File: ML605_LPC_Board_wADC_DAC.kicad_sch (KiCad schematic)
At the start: 19 parts, among them J1 ASP-134604-01, J10 Conn_02x06_Odd_Even, J11 Conn_02x06_Odd_Even, J12 Conn_02x06_Odd_Even, J2 Conn_01x03_Pin, J3 Conn_01x03_Pin, U1 LMV7219M7, U2 LMV7219M7, U3 NCV317

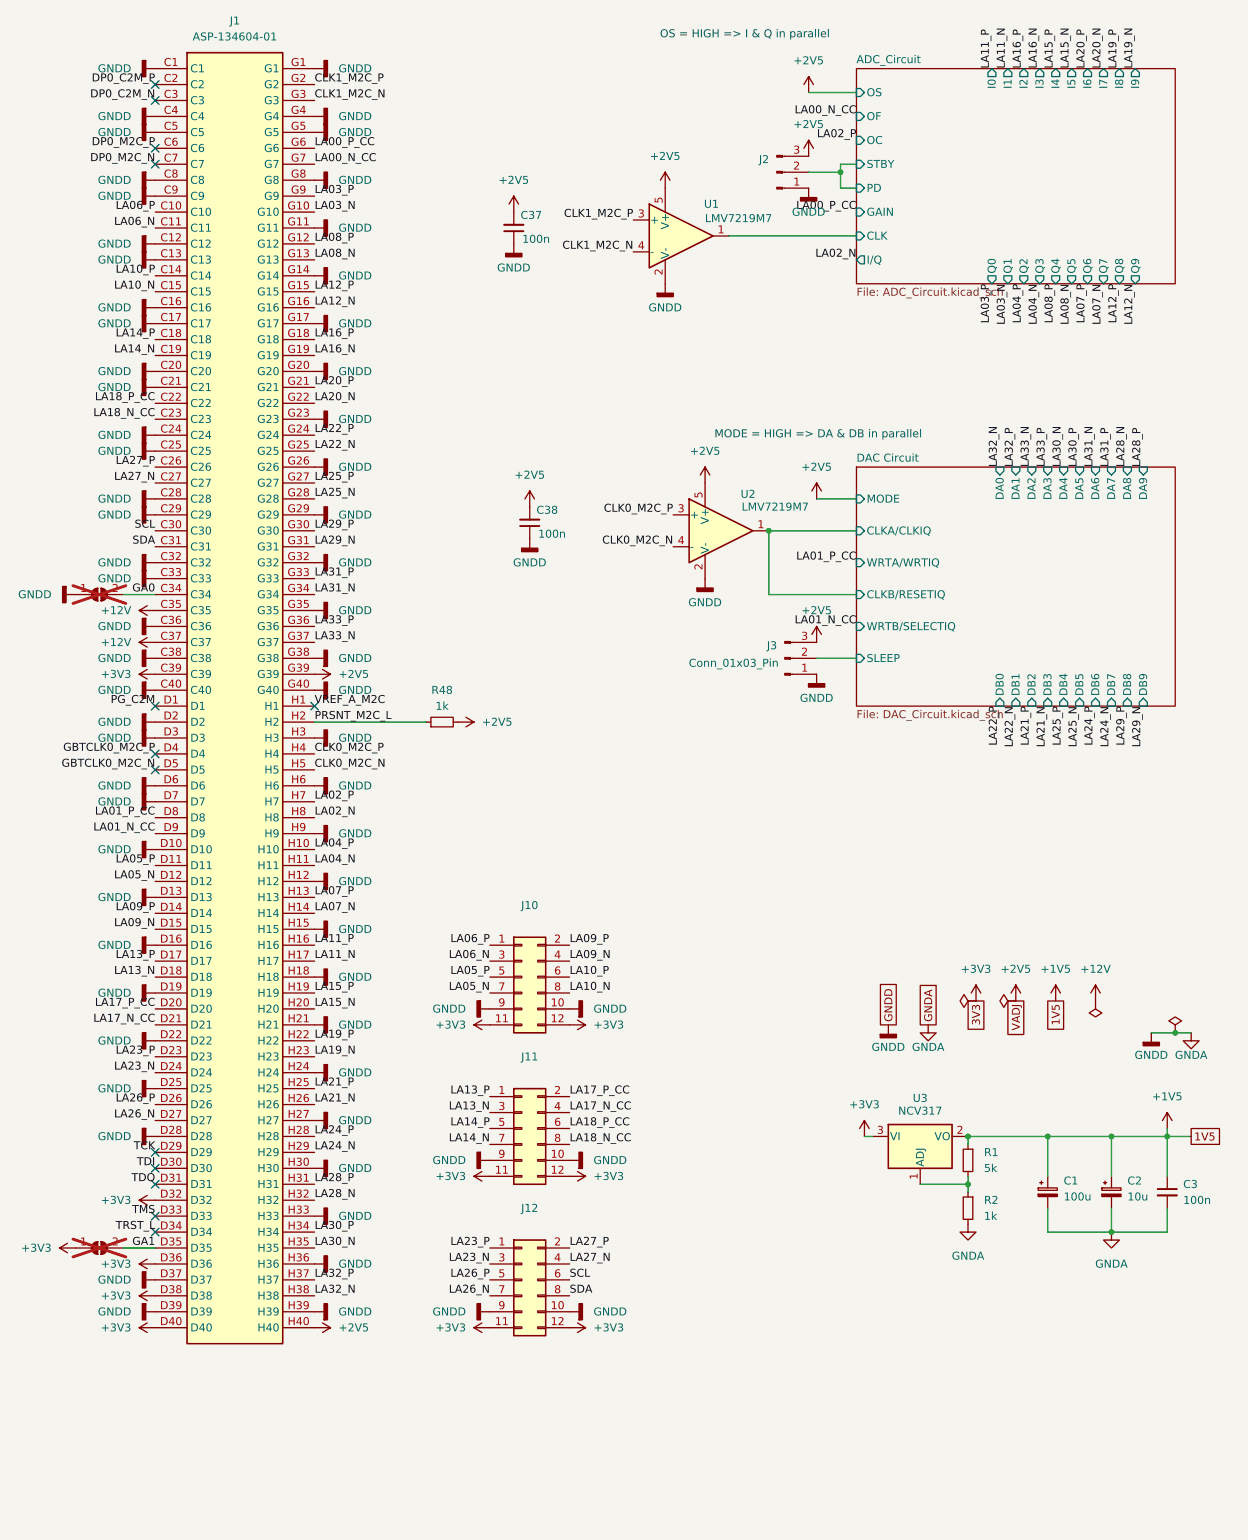
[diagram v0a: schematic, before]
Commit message: Second commit, routed digital data inputs of DAC
Now I have problems routing the WRTA & WRTB pins of the DAC. Will probably have to reassign some pins of the digital data inputs (potential solution: I could make the WRTA/WRTB pair be situated at LA29, and the DAC_DB input pins would have to be cascaded down. DAC_DB1/DAC_DB0 would then have to be moved to the other side of the LPC connector, probably where WRTA/WRTB are now, at LA26). It'll look weird in the pinout diagram, but at least it'll work (hopefully :@    )
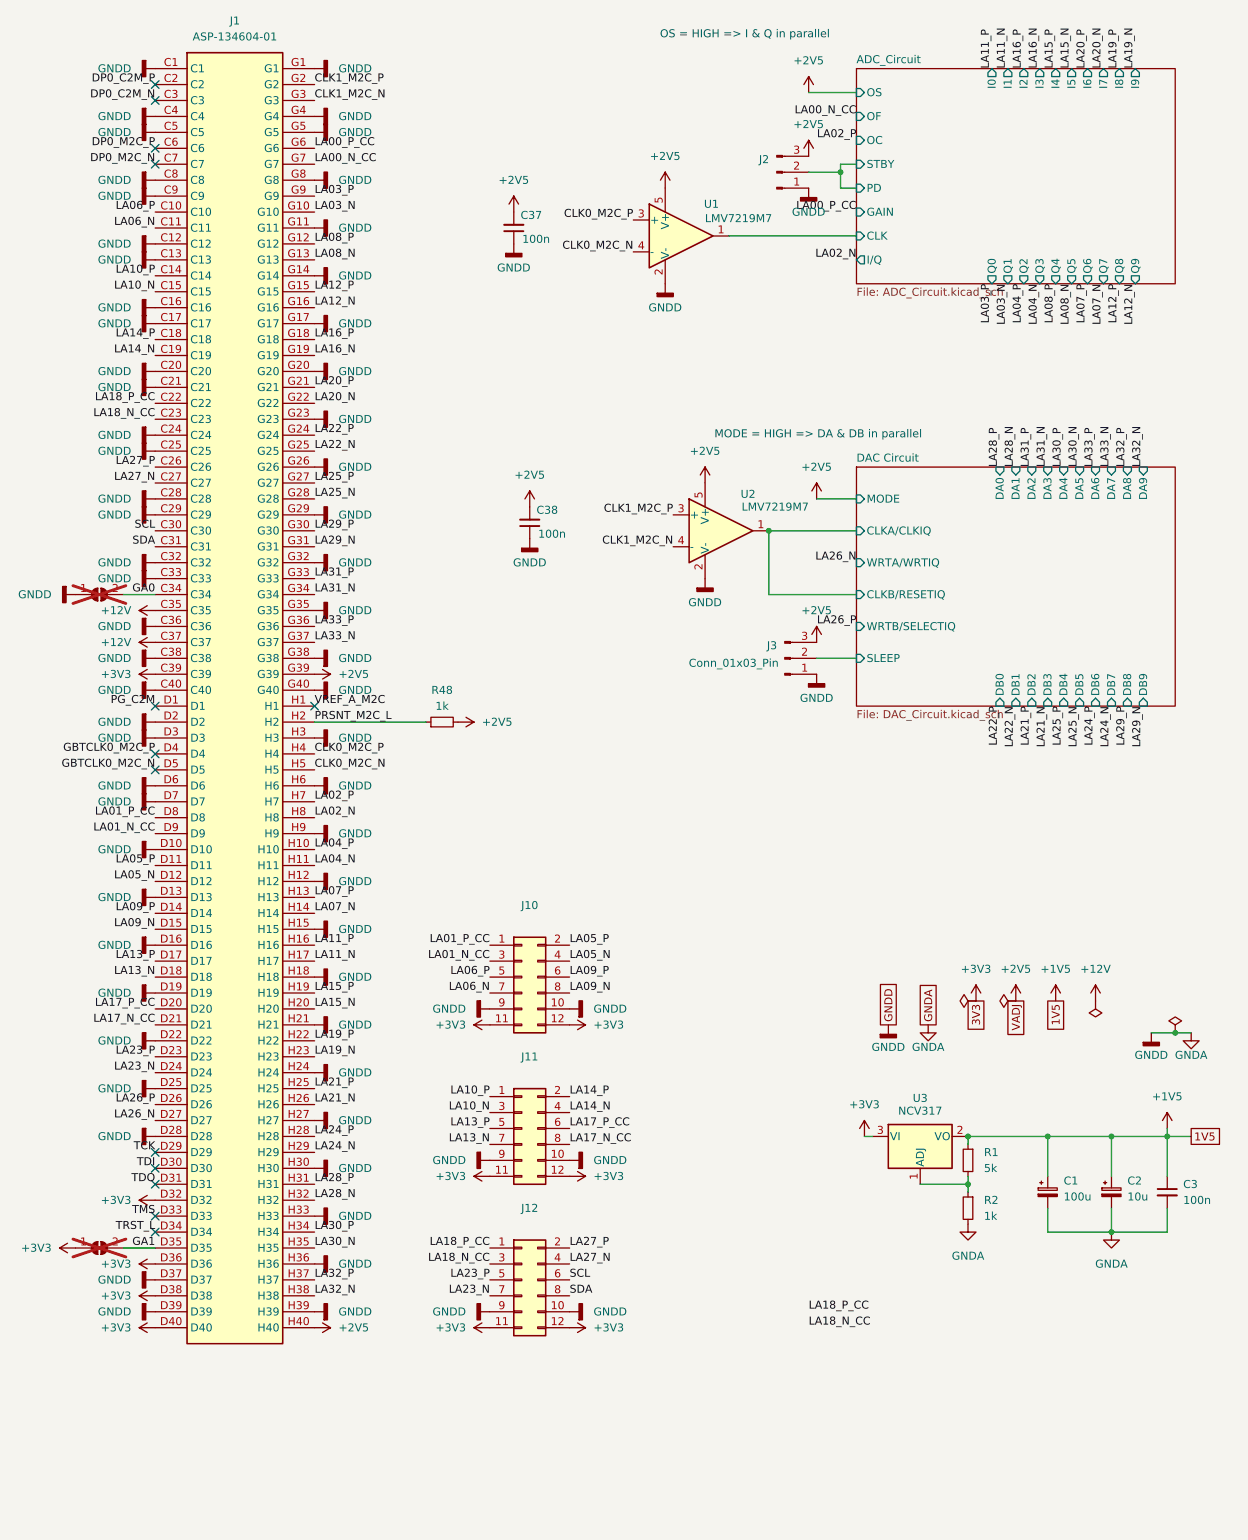
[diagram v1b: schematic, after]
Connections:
- net CLK0_M2C_N: now also U1.4 (-); no longer U2.4 (-)
- net CLK0_M2C_P: now also U1.3 (+); no longer U2.3 (+)
- net CLK1_M2C_N: now also U2.4 (-); no longer U1.4 (-)
- net CLK1_M2C_P: now also U2.3 (+); no longer U1.3 (+)
- net LA01_N_CC: now also J10.3 (Pin_3)
- net LA01_P_CC: now also J10.1 (Pin_1)
- net LA05_N: now also J10.4 (Pin_4); no longer J10.7 (Pin_7)
- net LA05_P: now also J10.2 (Pin_2); no longer J10.5 (Pin_5)
- net LA06_N: now also J10.7 (Pin_7); no longer J10.3 (Pin_3)
- net LA06_P: now also J10.5 (Pin_5); no longer J10.1 (Pin_1)
- net LA09_N: now also J10.8 (Pin_8); no longer J10.4 (Pin_4)
- net LA09_P: now also J10.6 (Pin_6); no longer J10.2 (Pin_2)
- net LA10_N: now also J11.3 (Pin_3); no longer J10.8 (Pin_8)
- net LA10_P: now also J11.1 (Pin_1); no longer J10.6 (Pin_6)
- net LA13_N: now also J11.7 (Pin_7); no longer J11.3 (Pin_3)
- net LA13_P: now also J11.5 (Pin_5); no longer J11.1 (Pin_1)
- net LA14_N: now also J11.4 (Pin_4); no longer J11.7 (Pin_7)
- net LA14_P: now also J11.2 (Pin_2); no longer J11.5 (Pin_5)
- net LA17_N_CC: now also J11.8 (Pin_8); no longer J11.4 (Pin_4)
- net LA17_P_CC: now also J11.6 (Pin_6); no longer J11.2 (Pin_2)
- net LA18_N_CC: now also J12.3 (Pin_3); no longer J11.8 (Pin_8)
- net LA18_P_CC: now also J12.1 (Pin_1); no longer J11.6 (Pin_6)
- net LA23_N: now also J12.7 (Pin_7); no longer J12.3 (Pin_3)
- net LA23_P: now also J12.5 (Pin_5); no longer J12.1 (Pin_1)
- net LA26_N: no longer J12.7 (Pin_7)
- net LA26_P: no longer J12.5 (Pin_5)

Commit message: The ADC/DAC part of the board is done
Now I just need to figure out how to do the GPIO breakout, but I have a lot more flexibility here. Ideally, I'd like to keep the PMOD connector format, however I'm not sure if that is going to be possible. If I can't do that due to routing issues, than I can probably just stick a 50-something pin header on the the top side of the board at the left edge, on the other side of the LPC connector and call it a day.
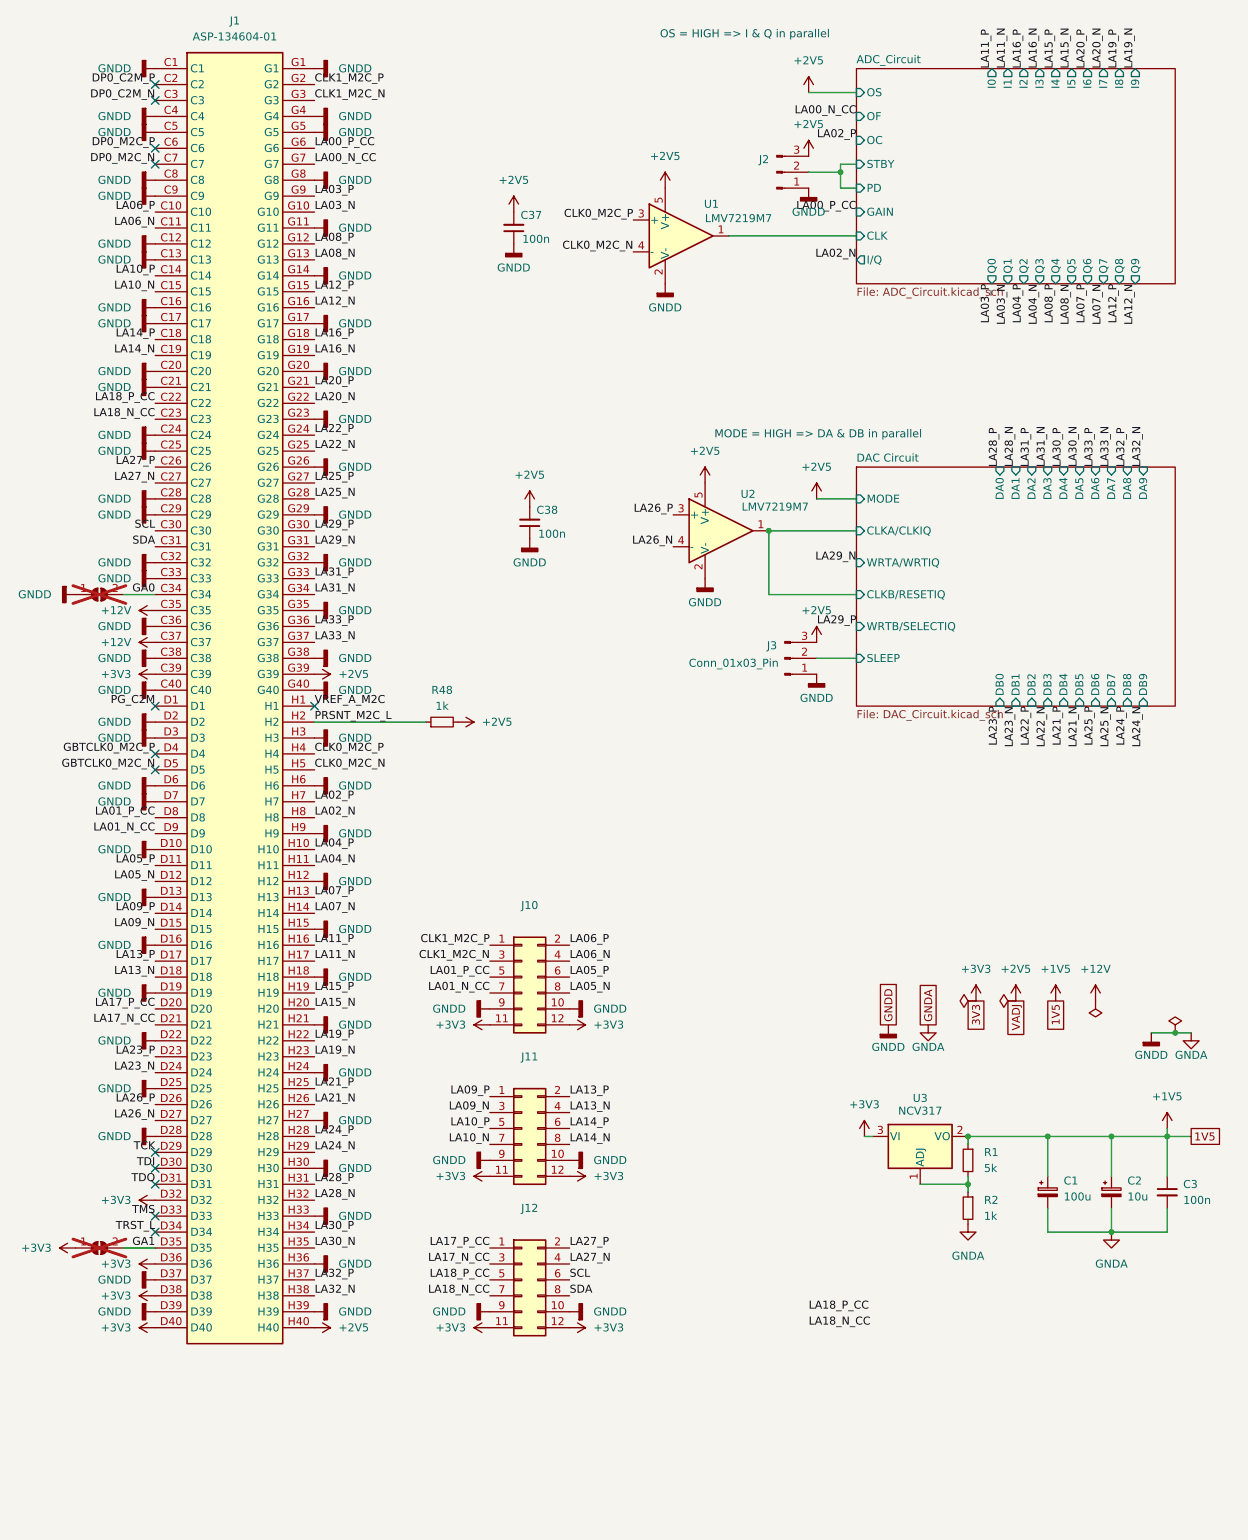
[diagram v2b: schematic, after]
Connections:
- net CLK1_M2C_N: now also J10.3 (Pin_3); no longer U2.4 (-)
- net CLK1_M2C_P: now also J10.1 (Pin_1); no longer U2.3 (+)
- net LA01_N_CC: now also J10.7 (Pin_7); no longer J10.3 (Pin_3)
- net LA01_P_CC: now also J10.5 (Pin_5); no longer J10.1 (Pin_1)
- net LA05_N: now also J10.8 (Pin_8); no longer J10.4 (Pin_4)
- net LA05_P: now also J10.6 (Pin_6); no longer J10.2 (Pin_2)
- net LA06_N: now also J10.4 (Pin_4); no longer J10.7 (Pin_7)
- net LA06_P: now also J10.2 (Pin_2); no longer J10.5 (Pin_5)
- net LA09_N: now also J11.3 (Pin_3); no longer J10.8 (Pin_8)
- net LA09_P: now also J11.1 (Pin_1); no longer J10.6 (Pin_6)
- net LA10_N: now also J11.7 (Pin_7); no longer J11.3 (Pin_3)
- net LA10_P: now also J11.5 (Pin_5); no longer J11.1 (Pin_1)
- net LA13_N: now also J11.4 (Pin_4); no longer J11.7 (Pin_7)
- net LA13_P: now also J11.2 (Pin_2); no longer J11.5 (Pin_5)
- net LA14_N: now also J11.8 (Pin_8); no longer J11.4 (Pin_4)
- net LA14_P: now also J11.6 (Pin_6); no longer J11.2 (Pin_2)
- net LA17_N_CC: now also J12.3 (Pin_3); no longer J11.8 (Pin_8)
- net LA17_P_CC: now also J12.1 (Pin_1); no longer J11.6 (Pin_6)
- net LA18_N_CC: now also J12.7 (Pin_7); no longer J12.3 (Pin_3)
- net LA18_P_CC: now also J12.5 (Pin_5); no longer J12.1 (Pin_1)
- net LA23_N: no longer J12.7 (Pin_7)
- net LA23_P: no longer J12.5 (Pin_5)
- net LA26_N: now also U2.4 (-)
- net LA26_P: now also U2.3 (+)

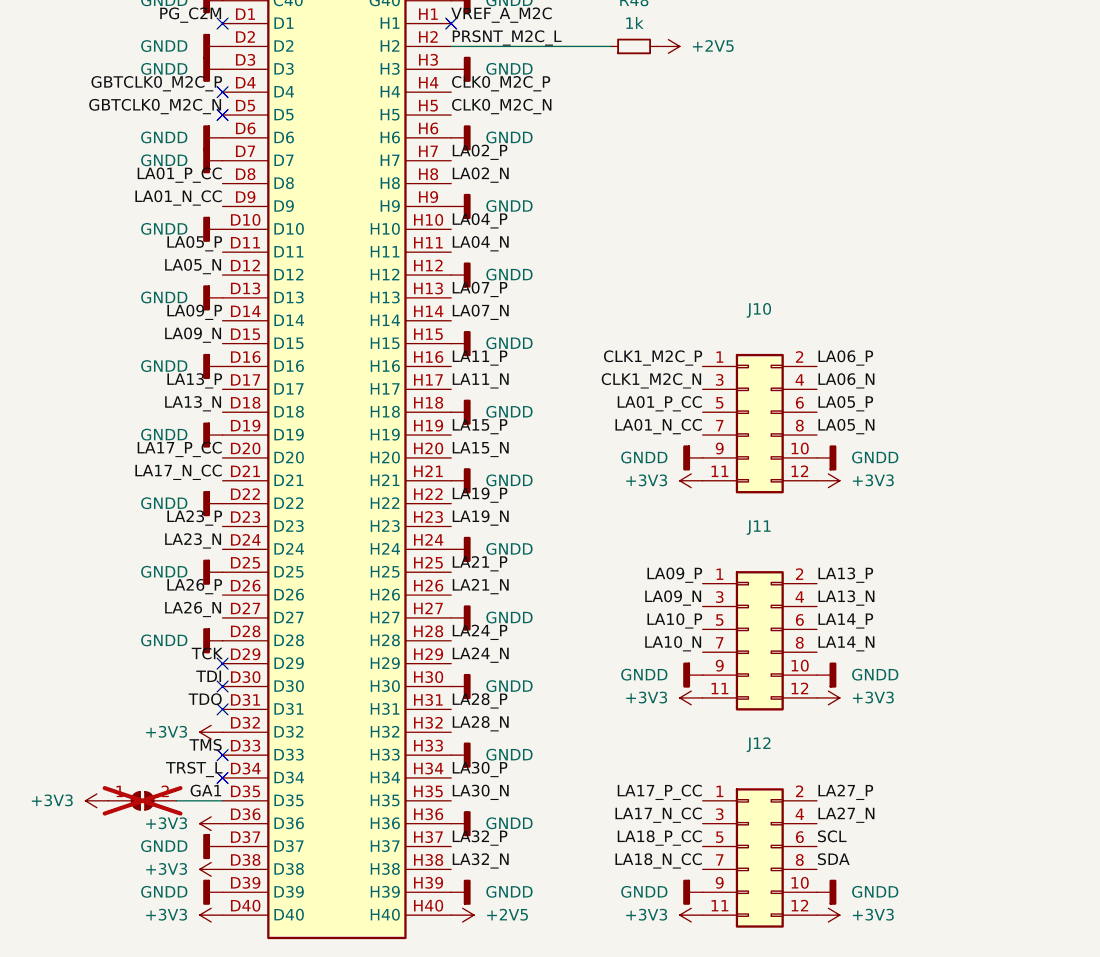
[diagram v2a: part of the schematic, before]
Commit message: Routing is done
Routing is finally done! Now I just need to add some silkscreen markings, maybe a label, order number placement, and I need to place some ground stitching vias here and there
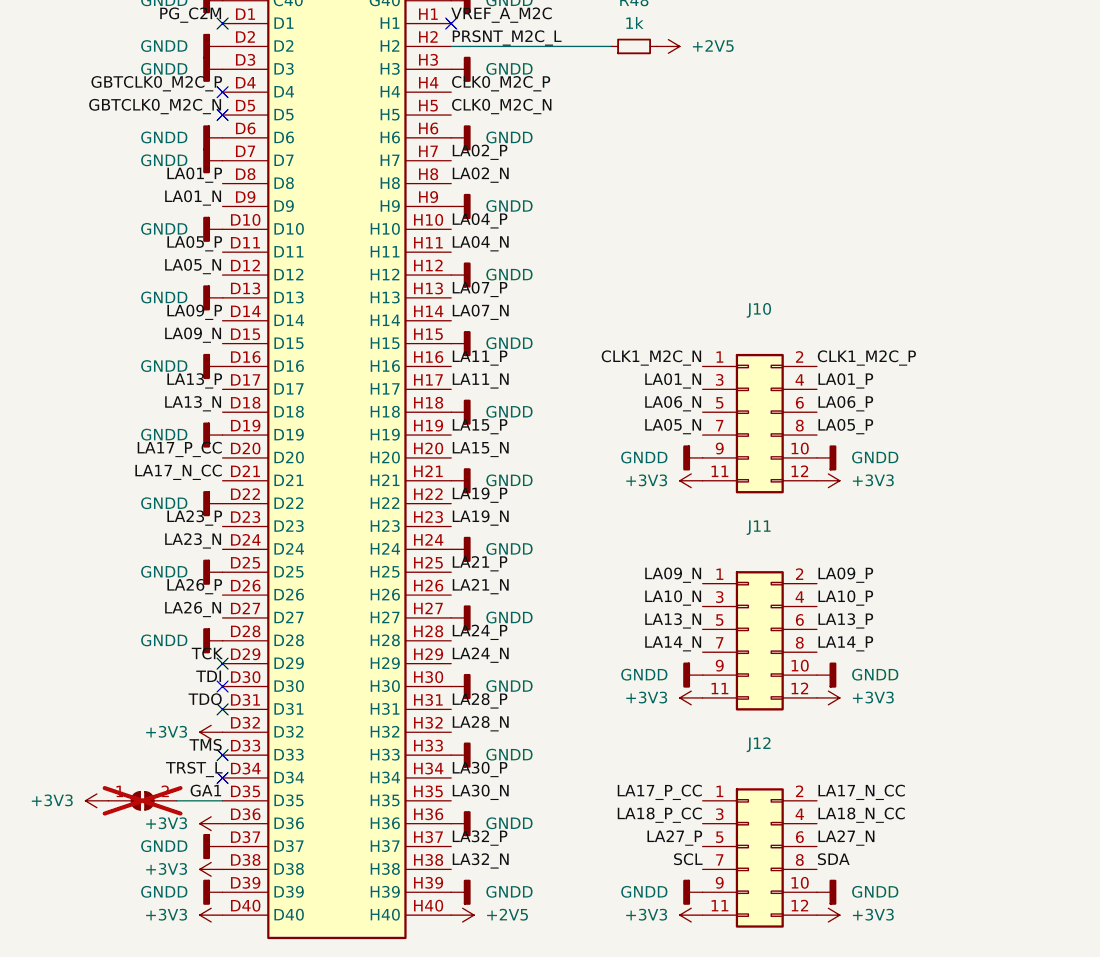
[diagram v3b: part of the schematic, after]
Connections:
- net CLK1_M2C_N: now also J10.1 (Pin_1); no longer J10.3 (Pin_3)
- net CLK1_M2C_P: now also J10.2 (Pin_2); no longer J10.1 (Pin_1)
- net LA05_N: now also J10.7 (Pin_7); no longer J10.8 (Pin_8)
- net LA05_P: now also J10.8 (Pin_8); no longer J10.6 (Pin_6)
- net LA06_N: now also J10.5 (Pin_5); no longer J10.4 (Pin_4)
- net LA06_P: now also J10.6 (Pin_6); no longer J10.2 (Pin_2)
- net LA09_N: now also J11.1 (Pin_1); no longer J11.3 (Pin_3)
- net LA09_P: now also J11.2 (Pin_2); no longer J11.1 (Pin_1)
- net LA10_N: now also J11.3 (Pin_3); no longer J11.7 (Pin_7)
- net LA10_P: now also J11.4 (Pin_4); no longer J11.5 (Pin_5)
- net LA13_N: now also J11.5 (Pin_5); no longer J11.4 (Pin_4)
- net LA13_P: now also J11.6 (Pin_6); no longer J11.2 (Pin_2)
- net LA14_N: now also J11.7 (Pin_7); no longer J11.8 (Pin_8)
- net LA14_P: now also J11.8 (Pin_8); no longer J11.6 (Pin_6)
- net LA17_N_CC: now also J12.2 (Pin_2); no longer J12.3 (Pin_3)
- net LA18_N_CC: now also J12.4 (Pin_4); no longer J12.7 (Pin_7)
- net LA18_P_CC: now also J12.3 (Pin_3); no longer J12.5 (Pin_5)
- net LA27_N: now also J12.6 (Pin_6); no longer J12.4 (Pin_4)
- net LA27_P: now also J12.5 (Pin_5); no longer J12.2 (Pin_2)
- net SCL: now also J12.7 (Pin_7); no longer J12.6 (Pin_6)
- net LA01_N_CC renamed LA01_N
- net LA01_N: now also J10.3 (Pin_3); no longer J10.7 (Pin_7)
- net LA01_P_CC renamed LA01_P
- net LA01_P: now also J10.4 (Pin_4); no longer J10.5 (Pin_5)
